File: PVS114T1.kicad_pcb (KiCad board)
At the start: 4 copper layers, 53.6 x 45.7 mm, 37 parts, among them J1 61FVXS-RSM1-GAN-TF_LF__SN_, J2 Conn_01x08_Male, U1 BU90T82-ZE2, U2 LT3473

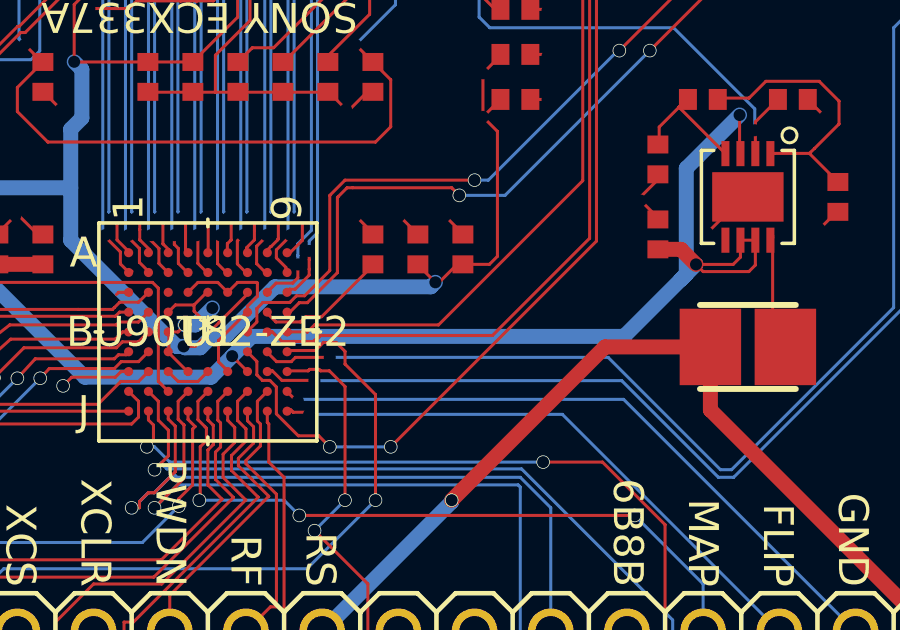
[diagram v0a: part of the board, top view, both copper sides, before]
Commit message: Conected unconected trace
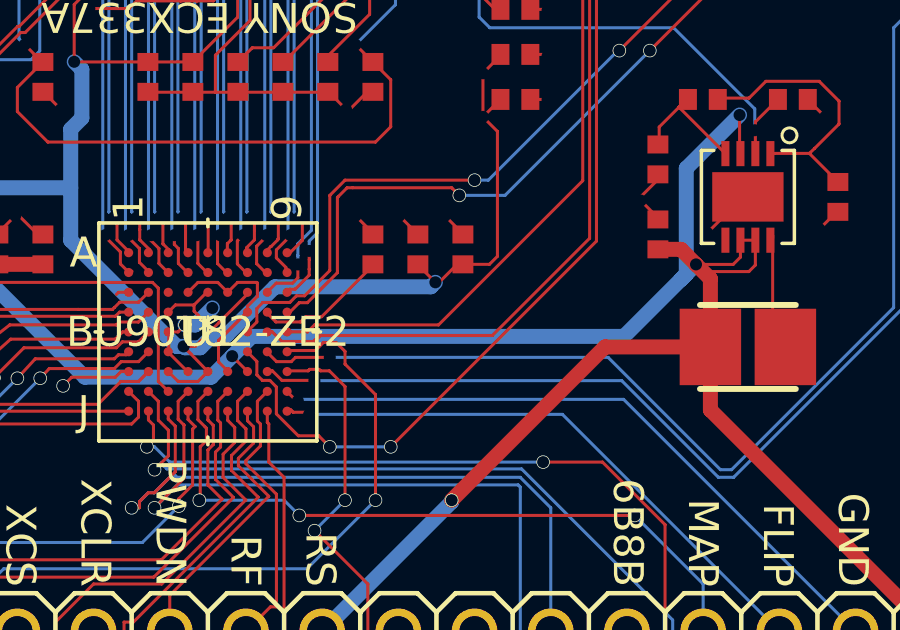
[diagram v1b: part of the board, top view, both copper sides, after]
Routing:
- net /PP1V8_LD1: track 119.0 -> 120.1 mm
- net /PP3V3_VO4: track 99.3 -> 98.6 mm
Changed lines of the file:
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@@
 (kicad_pcb (version 20211014) (generator pcbnew)
   (general
-    (thickness 4.69)
+    (thickness 3.0812)
   )
   (paper "A4")
@@
       (layer "F.Mask" (type "Top Solder Mask") (thickness 0.01))
       (layer "F.Cu" (type "copper") (thickness 0.035))
-      (layer "dielectric 1" (type "core") (thickness 1.51) (material "FR4") (epsilon_r 4.5) (loss_tangent 0.02))
-      (layer "In1.Cu" (type "copper") (thickness 0.035))
-      (layer "dielectric 2" (type "prepreg") (thickness 1.51) (material "FR4") (epsilon_r 4.5) (loss_tangent 0.02))
-      (layer "In2.Cu" (type "copper") (thickness 0.035))
+      (layer "dielectric 1" (type "core") (thickness 0.2104) (material "FR4") (epsilon_r 4.5) (loss_tangent 0.02))
+      (layer "In1.Cu" (type "copper") (thickness 0.0152))
+      (layer "dielectric 2" (type "prepreg") (thickness 1.065) (material "FR4") (epsilon_r 4.5) (loss_tangent 0.02))
+      (layer "In2.Cu" (type "copper") (thickness 0.0152))
       (layer "dielectric 3" (type "core") (thickness 1.51) (material "FR4") (epsilon_r 4.5) (loss_tangent 0.02))
-      (layer "B.Cu" (type "copper") (thickness 0.035))
+      (layer "B.Cu" (type "copper") (thickness 0.2104))
       (layer "B.Mask" (type "Bottom Solder Mask") (thickness 0.01))
       (layer "B.Paste" (type "Bottom Solder Paste"))
@@
   (segment (start 151.99106 114.90706) (end 151.638 114.554) (width 0.1016) (layer "F.Cu") (net 3))
   (segment (start 157.7594 123.8758) (end 158.242 124.3584) (width 0.1016) (layer "F.Cu") (net 3))
+  (segment (start 148.59 132.36448) (end 147.78228 131.52628) (width 0.1016) (layer "F.Cu") (net 3))
   (segment (start 142.546438 117.295562) (end 142.665818 117.295562) (width 0.1016) (layer "F.Cu") (net 3))
   (segment (start 147.2692 130.38328) (end 147.50754 130.14494) (width 0.1016) (layer "F.Cu") (net 3))
@@
   (segment (start 123.74951 144.76222) (end 146.12112 144.76222) (width 0.1016) (layer "B.Cu") (net 70))
   (segment (start 128.5875 124.67336) (end 127.54102 125.71984) (width 0.5) (layer "F.Cu") (net 71))
+  (segment (start 165.3413 131.54406) (end 165.3413 129.2733) (width 0.5) (layer "F.Cu") (net 71))
   (segment (start 166.31412 125.07214) (end 166.34206 125.10008) (width 0.1016) (layer "F.Cu") (net 71))
   (segment (start 128.5875 123.04268) (end 130.72618 120.904) (width 0.5) (layer "F.Cu") (net 71))
+  (segment (start 165.3413 129.2733) (end 164.86124 128.79324) (width 0.5) (layer "F.Cu") (net 71))
   (segment (start 127.53086 125.71476) (end 127.54102 125.7173) (width 0.1016) (layer "F.Cu") (net 71))
   (segment (start 165.3413 133.64464) (end 172.72 141.02334) (width 0.5) (layer "F.Cu") (net 71))
@@
   (via (at 139.7127 128.7907) (size 0.45) (drill 0.4) (layers "F.Cu" "B.Cu") (net 71))
   (via (at 149.40026 131.8514) (size 0.19812) (drill 0.4) (layers "F.Cu" "B.Cu") (net 71))
-  (segment (start 142.2726 131.3506) (end 139.7127 128.7907) (width 0.1016) (layer "In1.Cu") (net 71))
   (segment (start 152.4 141.02334) (end 156.718 136.70534) (width 0.5) (layer "B.Cu") (net 71))
   (segment (start 164.35324 129.30124) (end 164.53716 129.11732) (width 0.5) (layer "B.Cu") (net 71))
